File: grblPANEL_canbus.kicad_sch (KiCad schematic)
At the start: 12 parts, among them J301 Conn_01x02, U301 SN65HVD230

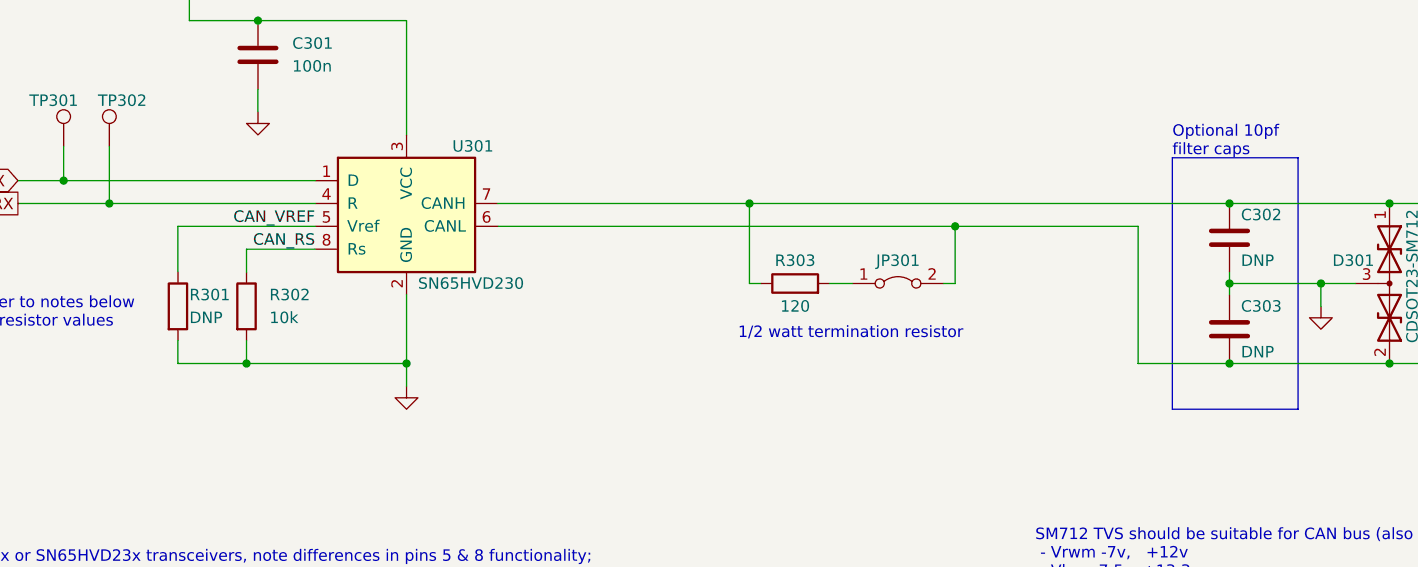
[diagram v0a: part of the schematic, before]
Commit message: Board changes for Rev B
Import changes from schematic.

Place and route changes from schematic:
Headers for serial console.
DNP components to v7 format.
Power status components.
LEDs to bottom side, plus silkscreen.

Update schematic page settings (RevB).

Update PCB page settings (RevB).

Silkscreen & test point tweaks.
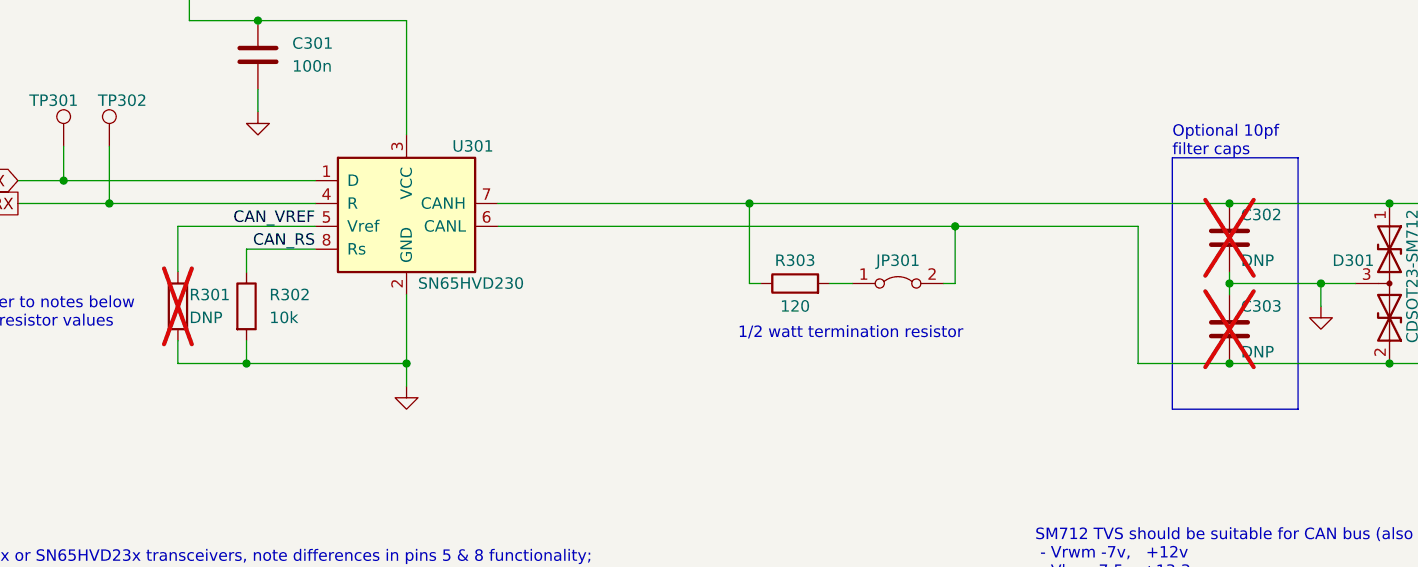
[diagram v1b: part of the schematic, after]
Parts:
- C302, C303, R301: now not fitted
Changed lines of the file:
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@@
     (title "grblPANEL")
     (date "2022-12-12")
-    (rev "0.1")
+    (rev "B")
     (company "dresco")
   )
@@
   )
   (symbol (lib_id "Device:C") (at 191.77 82.55 0) (unit 1)
-    (in_bom yes) (on_board yes) (dnp no)
+    (in_bom yes) (on_board yes) (dnp yes)
     (property "Reference" "C303" (at 193.04 80.01 0)
       (effects (font (size 1.27 1.27)) (justify left))
@@
   )
   (symbol (lib_id "Device:C") (at 191.77 72.39 0) (unit 1)
-    (in_bom yes) (on_board yes) (dnp no)
+    (in_bom yes) (on_board yes) (dnp yes)
     (property "Reference" "C302" (at 193.04 69.85 0)
       (effects (font (size 1.27 1.27)) (justify left))
@@
   )
   (symbol (lib_id "Device:R") (at 74.93 80.01 0) (unit 1)
-    (in_bom yes) (on_board yes) (dnp no)
+    (in_bom yes) (on_board yes) (dnp yes)
     (property "Reference" "R301" (at 76.2 78.74 0)
       (effects (font (size 1.27 1.27)) (justify left))
